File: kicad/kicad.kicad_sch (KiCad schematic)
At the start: 0 parts

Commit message: added controller
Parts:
- added A1: Arduino_Uno_R3_SMD_Shield, PCM_arduino-library:Arduino_Uno_R3_Shield, symbol PCM_arduino-library:Arduino_Uno_R3_SMD_Shield
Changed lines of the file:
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@@
+		)
+	)
+	(symbol
+		(lib_id "PCM_arduino-library:Arduino_Uno_R3_SMD_Shield")
+		(at 156.21 93.98 0)
+		(unit 1)
+		(exclude_from_sim no)
+		(in_bom yes)
+		(on_board yes)
+		(dnp no)
+		(fields_autoplaced yes)
+		(property "Reference" "A1"
+			(at 156.21 58.42 0)
+			(effects
+				(font
+					(size 1.524 1.524)
+				)
+			)
+		)
+		(property "Value" "Arduino_Uno_R3_SMD_Shield"
+			(at 156.21 60.96 0)
+			(effects
+				(font
+					(size 1.524 1.524)
+				)
+			)
+		)
+		(property "Footprint" "PCM_arduino-library:Arduino_Uno_R3_Shield"
+			(at 156.21 132.08 0)
+			(effects
+				(font
+					(size 1.524 1.524)
+				)
+				(hide yes)
+			)
+		)
+		(property "Datasheet" "https://docs.arduino.cc/hardware/uno-rev3-smd"
+			(at 156.21 128.27 0)
+			(effects
+				(font
+					(size 1.524 1.524)
+				)
+				(hide yes)
+			)
+		)
+		(property "Description" "Shield for Arduino UNO R3 SMD"
+			(at 156.21 93.98 0)
+			(effects
+				(font
+					(size 1.27 1.27)
+				)
+				(hide yes)
+			)
+		)
+		(pin "D12"
+		)
+		(pin "D6"
+		)
+		(pin "GND3"
+		)
+		(pin "A5"
+		)
+		(pin "MISO"
+		)
+		(pin "A4"
+		)
+		(pin "3V3"
+		)
+		(pin "D13"
+		)
+		(pin "D1"
+		)
+		(pin "D8"
+		)
+		(pin "AREF"
+		)
+		(pin "RST1"
+		)
+		(pin "SCK"
+		)
+		(pin "D10"
+		)
+		(pin "VIN"
+		)
+		(pin "GND2"
+		)
+		(pin "A0"
+		)
+		(pin "D9"
+		)
+		(pin "GND4"
+		)
+		(pin "SCL"
+		)
+		(pin "A2"
+		)
+		(pin "RST2"
+		)
+		(pin "MOSI"
+		)
+		(pin "5V1"
+		)
+		(pin "A3"
+		)
+		(pin "D0"
+		)
+		(pin "D5"
+		)
+		(pin "SDA"
+		)
+		(pin "A1"
+		)
+		(pin "D7"
+		)
+		(pin "IORF"
+		)
+		(pin "D2"
+		)
+		(pin "D3"
+		)
+		(pin "5V2"
+		)
+		(pin "D4"
+		)
+		(pin "D11"
+		)
+		(pin "GND1"
+		)
+		(instances
+			(project ""
+				(path "/361dfde8-db82-4f79-b593-288fe0fd1919"
+					(reference "A1")
+					(unit 1)
+				)
+			)
 		)
 	)

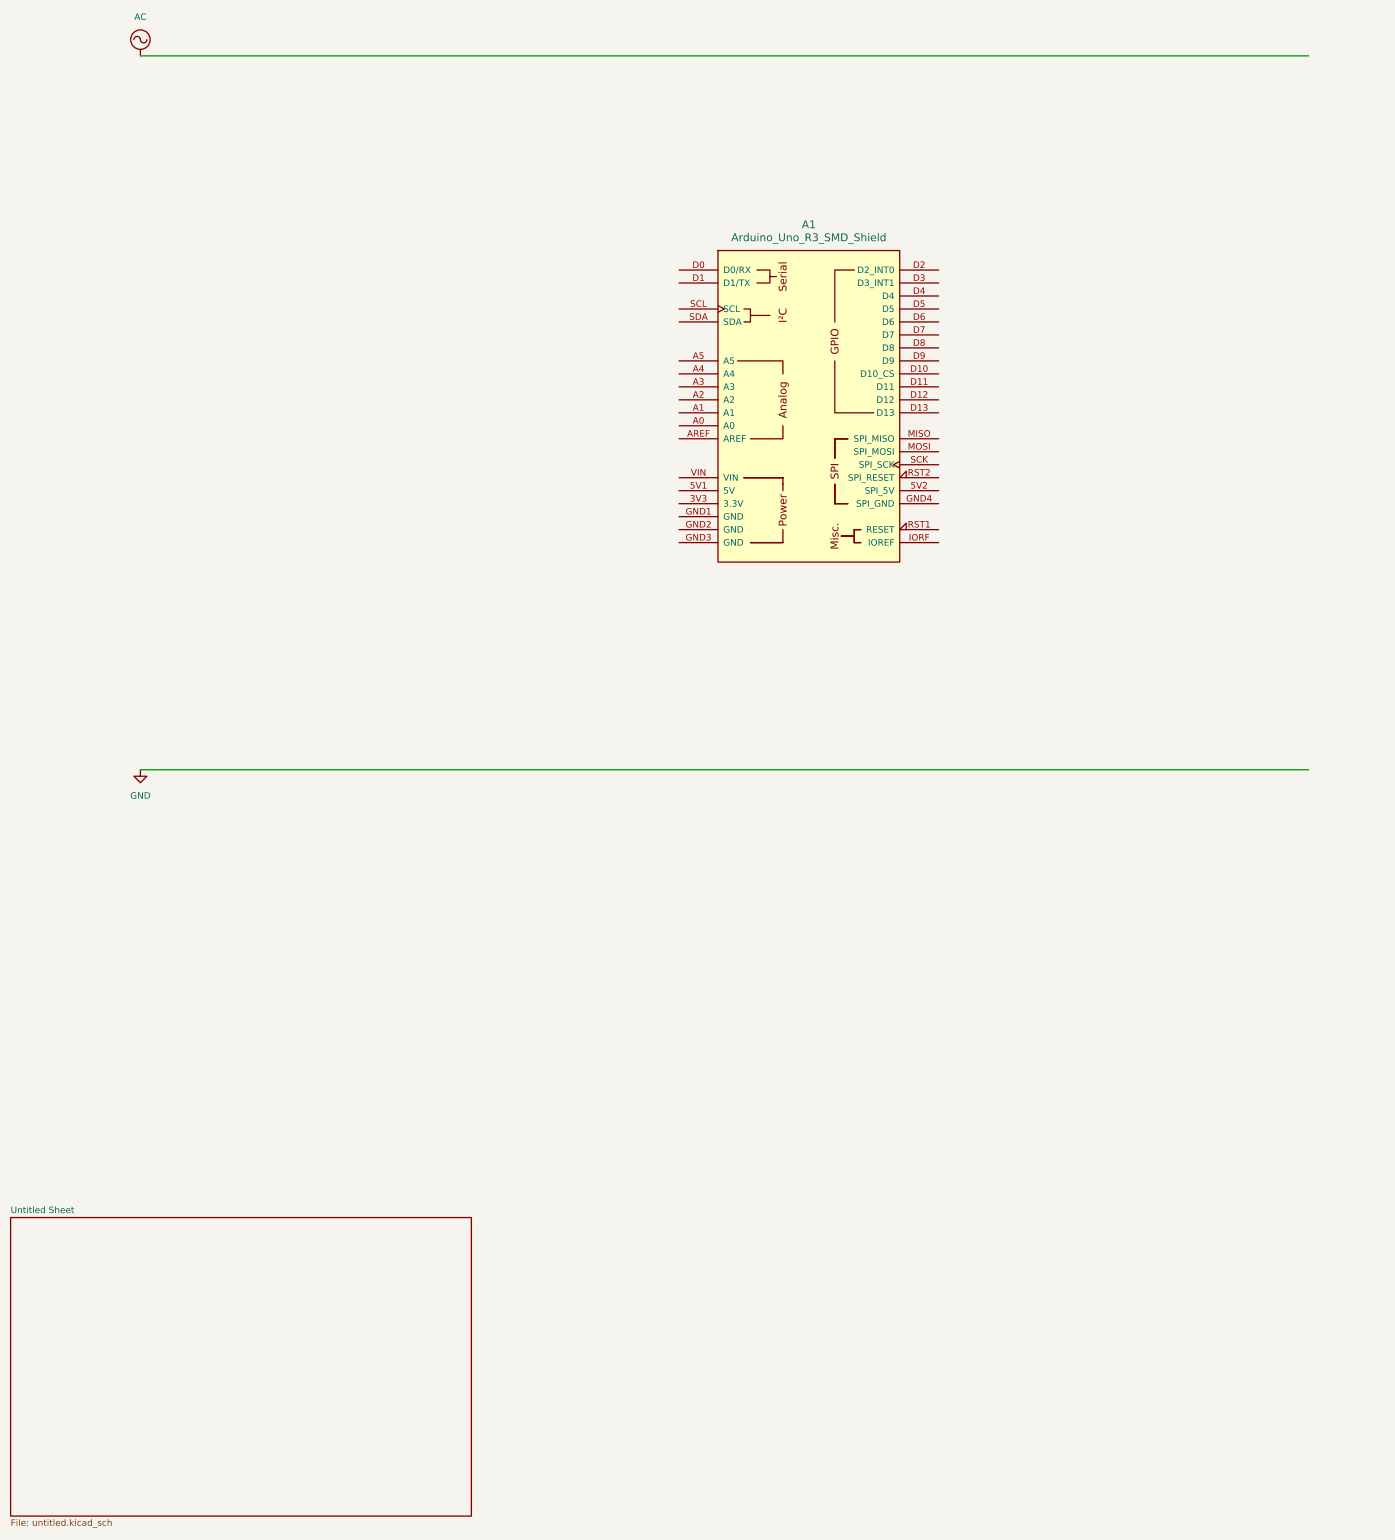
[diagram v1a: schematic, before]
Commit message: shift register wiring cleanup
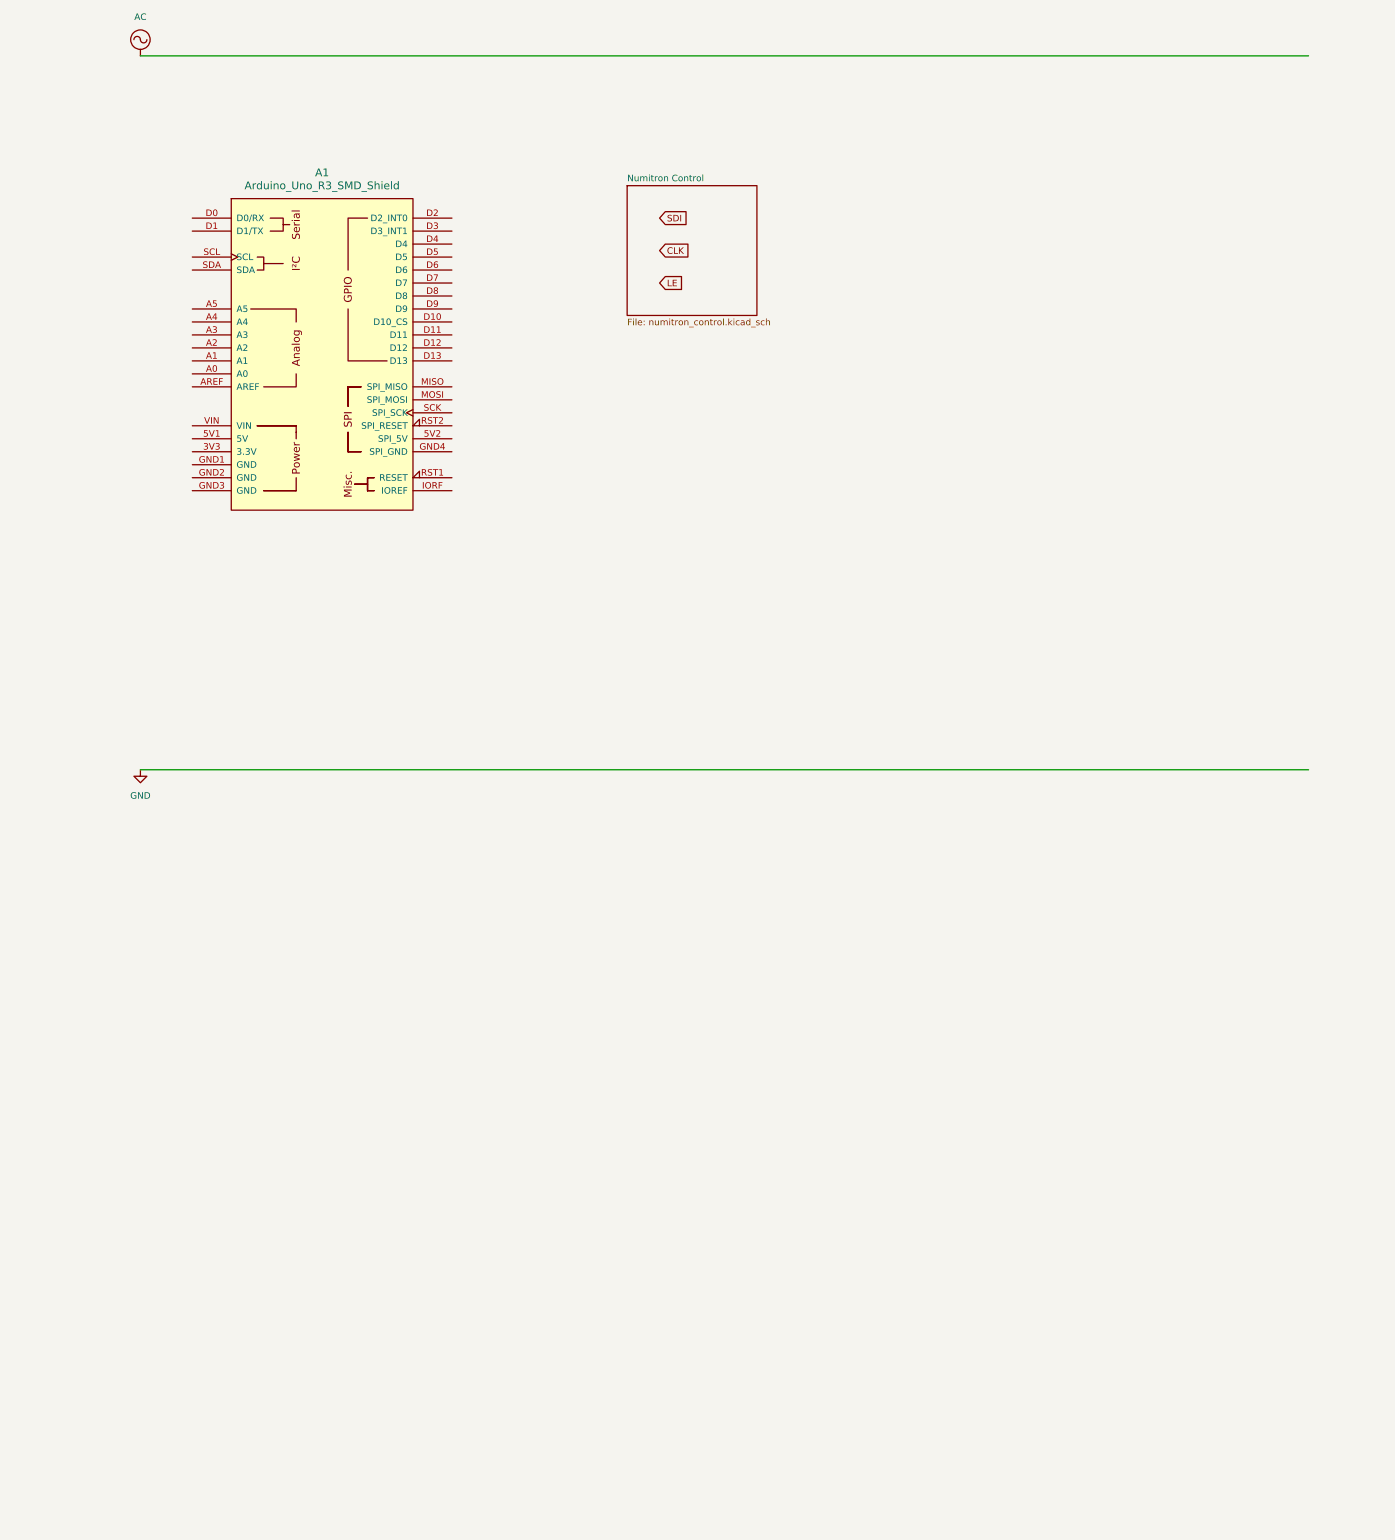
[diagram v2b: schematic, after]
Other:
- removed sheet Untitled Sheet
- added sheet Numitron Control (numitron_control.kicad_sch)
- moved on the sheet: A1
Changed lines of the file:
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@@
+		)
+	)
+	(global_label "LE"
+		(shape input)
+		(at 127 69.85 0)
+		(fields_autoplaced yes)
+		(effects
+			(font
+				(size 1.27 1.27)
+			)
+			(justify left)
+		)
+		(property "Intersheetrefs" "${INTERSHEET_REFS}"
+			(at 132.1623 69.85 0)
+			(effects
+				(font
+					(size 1.27 1.27)
+				)
+				(justify left)
+				(hide yes)
+			)
+		)
+	)
+	(global_label "CLK"
+		(shape input)
+		(at 127 63.5 0)
+		(fields_autoplaced yes)
+		(effects
+			(font
+				(size 1.27 1.27)
+			)
+			(justify left)
+		)
+		(property "Intersheetrefs" "${INTERSHEET_REFS}"
+			(at 133.5533 63.5 0)
+			(effects
+				(font
+					(size 1.27 1.27)
+				)
+				(justify left)
+				(hide yes)
+			)
+		)
+	)
+	(global_label "SDI"
+		(shape input)
+		(at 127 57.15 0)
+		(fields_autoplaced yes)
+		(effects
+			(font
+				(size 1.27 1.27)
+			)
+			(justify left)
+		)
+		(property "Intersheetrefs" "${INTERSHEET_REFS}"
+			(at 133.0695 57.15 0)
+			(effects
+				(font
+					(size 1.27 1.27)
+				)
+				(justify left)
+				(hide yes)
+			)
 		)
 	)
@@
 	(symbol
 		(lib_id "PCM_arduino-library:Arduino_Uno_R3_SMD_Shield")
-		(at 156.21 93.98 0)
+		(at 60.96 83.82 0)
 		(unit 1)
 		(exclude_from_sim no)
@@
 		(fields_autoplaced yes)
 		(property "Reference" "A1"
-			(at 156.21 58.42 0)
+			(at 60.96 48.26 0)
 			(effects
 				(font
@@
 		)
 		(property "Value" "Arduino_Uno_R3_SMD_Shield"
-			(at 156.21 60.96 0)
+			(at 60.96 50.8 0)
 			(effects
 				(font
@@
 		)
 		(property "Footprint" "PCM_arduino-library:Arduino_Uno_R3_Shield"
-			(at 156.21 132.08 0)
+			(at 60.96 121.92 0)
 			(effects
 				(font
@@
 		)
 		(property "Datasheet" "https://docs.arduino.cc/hardware/uno-rev3-smd"
-			(at 156.21 128.27 0)
+			(at 60.96 118.11 0)
 			(effects
 				(font
@@
 		)
 		(property "Description" "Shield for Arduino UNO R3 SMD"
-			(at 156.21 93.98 0)
+			(at 60.96 83.82 0)
 			(effects
 				(font
@@
 	)
 	(sheet
-		(at 0 252.73)
-		(size 90.17 58.42)
+		(at 120.65 50.8)
+		(size 25.4 25.4)
 		(fields_autoplaced yes)
 		(stroke
@@
 			(color 0 0 0 0.0000)
 		)
-		(property "Sheetname" "Untitled Sheet"
-			(at 0 252.0184 0)
+		(property "Sheetname" "Numitron Control"
+			(at 120.65 50.0884 0)
 			(effects
 				(font
@@
 			)
 		)
-		(property "Sheetfile" "untitled.kicad_sch"
-			(at 0 311.7346 0)
-			(effects
-				(font
+		(property "Sheetfile" "numitron_control.kicad_sch"
+			(at 120.65 76.7846 0)
+			(effects
+				(font

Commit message: added voltage regulators, changed bit register
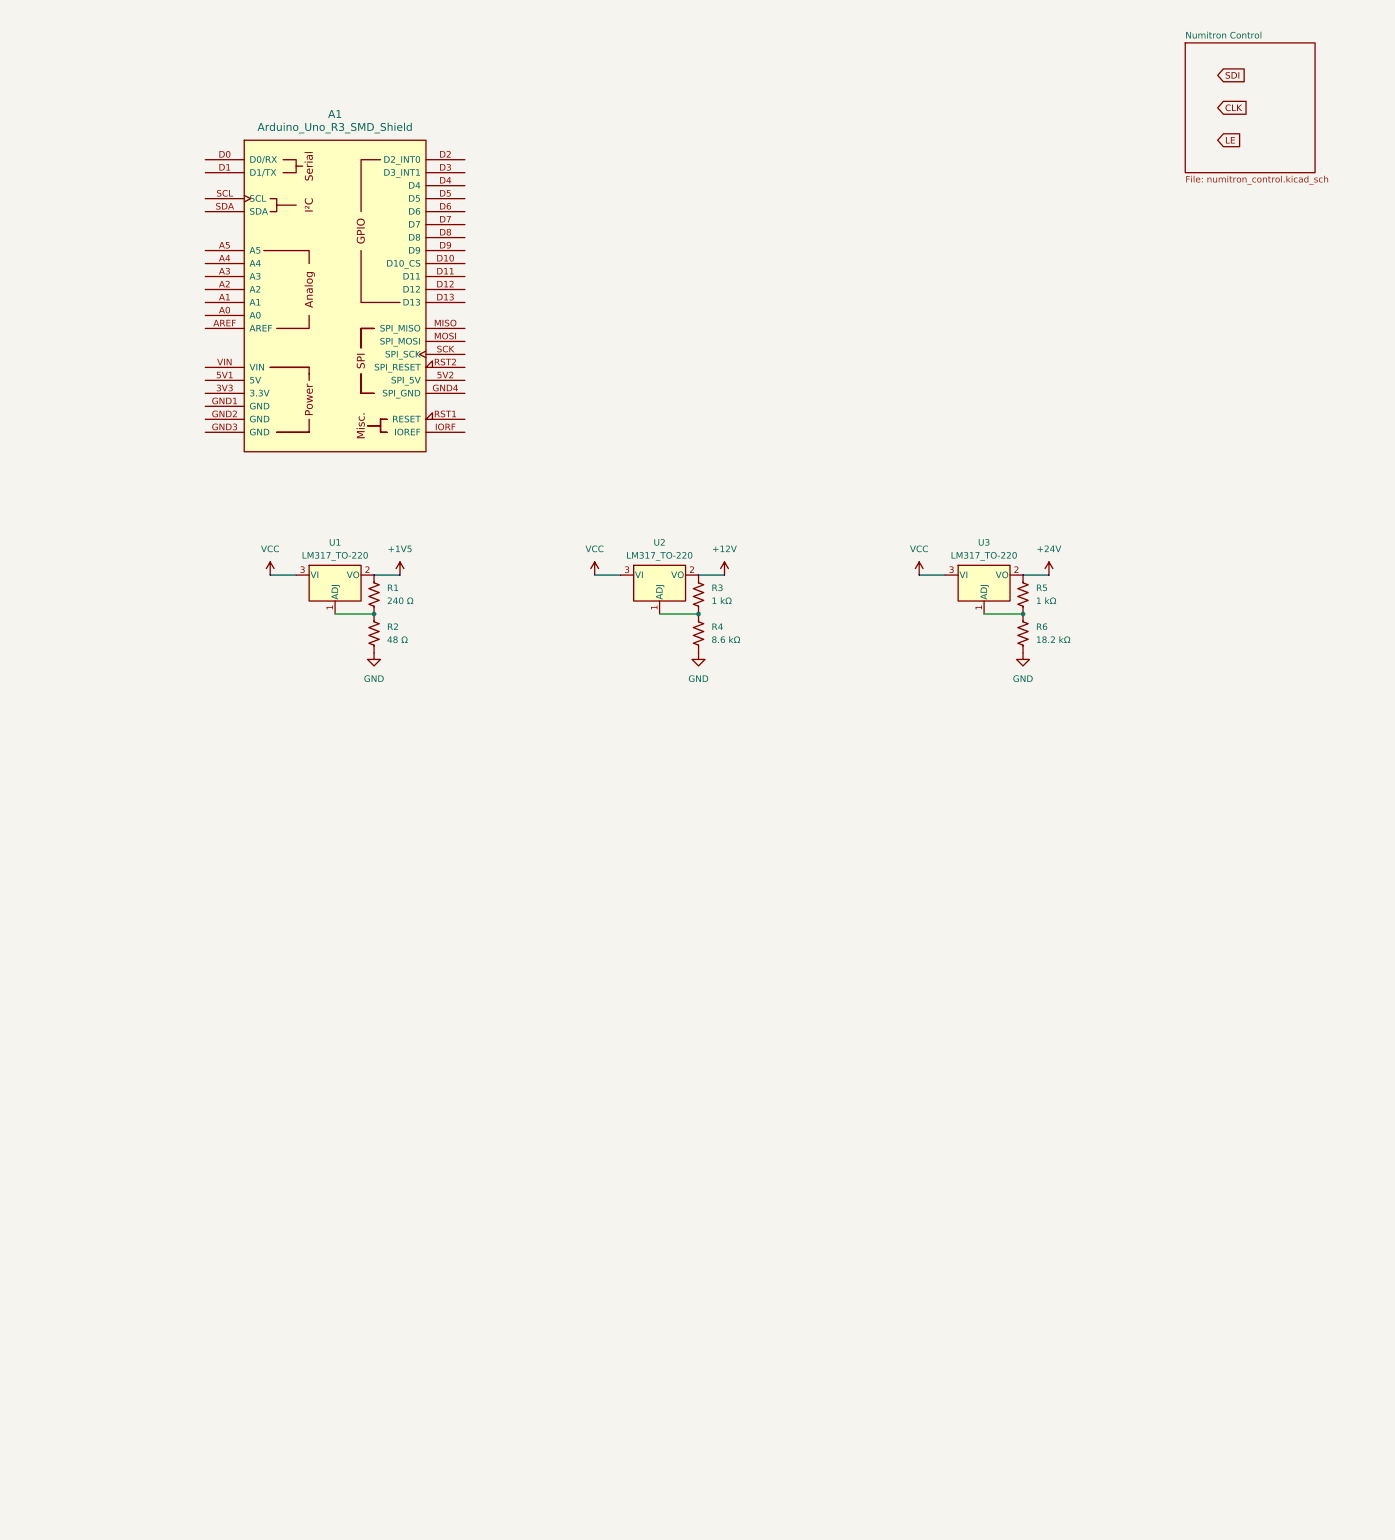
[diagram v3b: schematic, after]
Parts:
- added R1: 240 Ω, symbol Device:R_US
- added R2: 48 Ω, symbol Device:R_US
- added R3, R5: 1 kΩ, symbol Device:R_US
- added R4: 8.6 kΩ, symbol Device:R_US
- added R6: 18.2 kΩ, symbol Device:R_US
- added U1, U2, U3: LM317_TO-220, Package_TO_SOT_THT:TO-220-3_Vertical, symbol Regulator_Linear:LM317_TO-220
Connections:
- net GND: now also R2.2, R4.2, R6.2
- new net: R1.2, R2.1, U1.1 (ADJ)
- new net: R1.1, U1.2 (VO)
- new net: R3.2, R4.1, U2.1 (ADJ)
- new net: R3.1, U2.2 (VO)
- new net: R5.2, R6.1, U3.1 (ADJ)
- new net: R5.1, U3.2 (VO)
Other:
- moved on the sheet: A1
